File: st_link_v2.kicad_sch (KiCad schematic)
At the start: 17 parts, among them SW401 STLINK_RST, U401 STM32F103CBTx, Y401 8MHz (7pF)

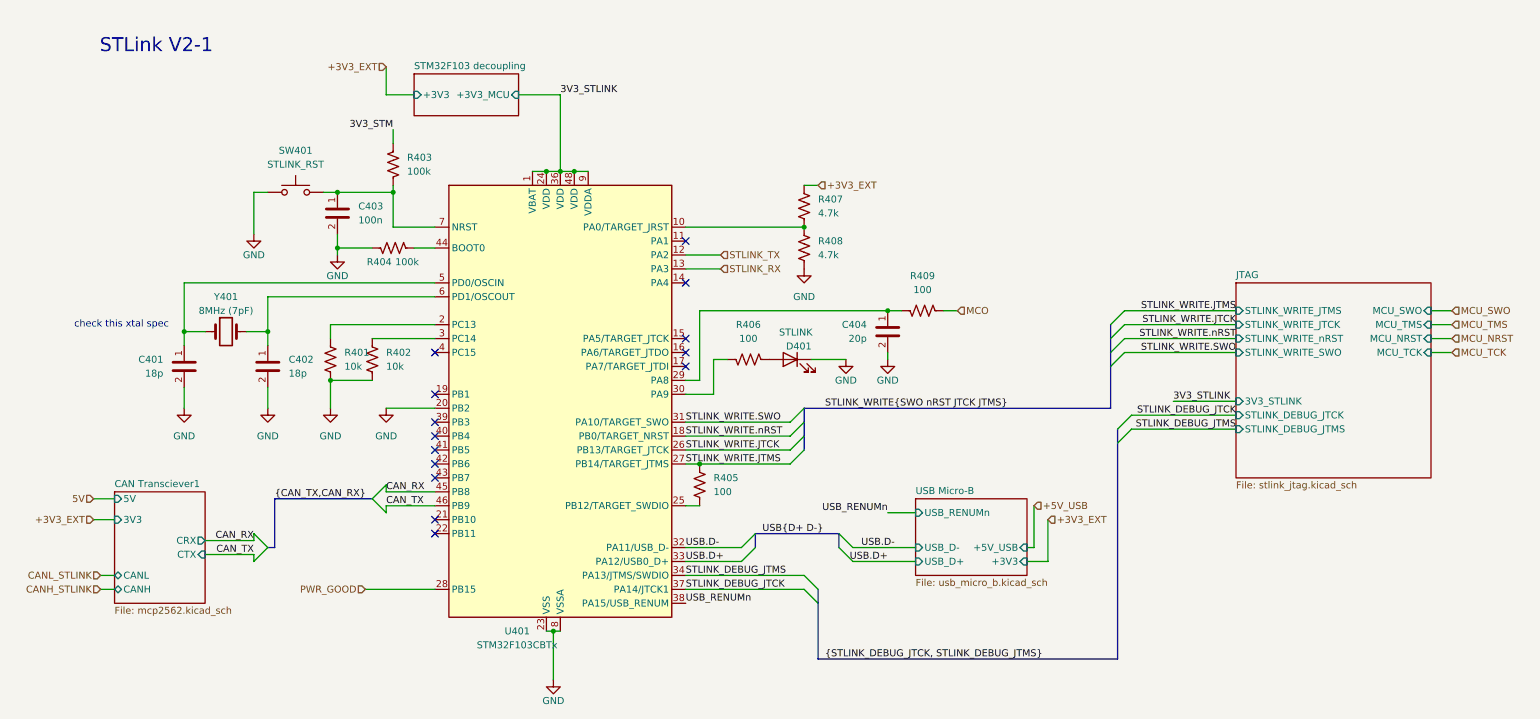
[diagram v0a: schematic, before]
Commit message: jk im stupid forgot to route the flash
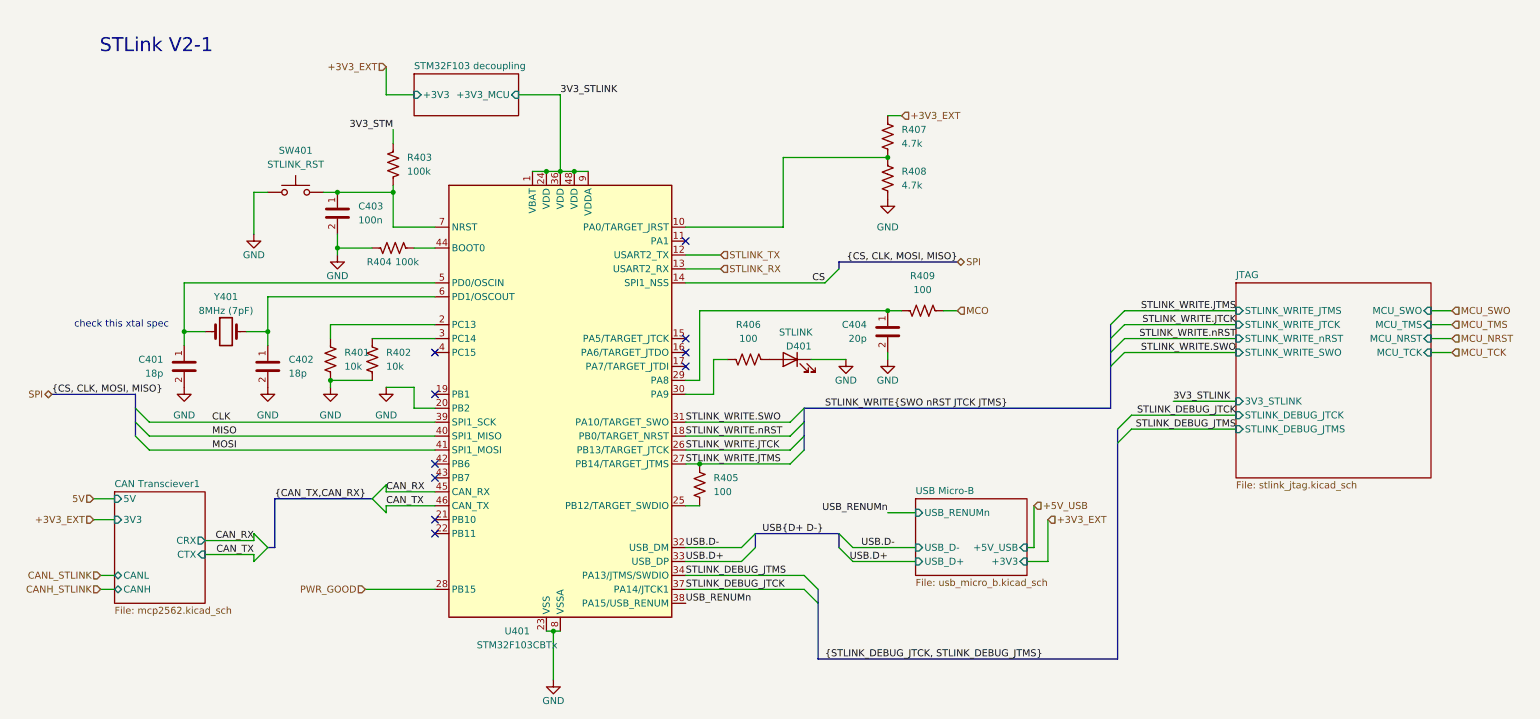
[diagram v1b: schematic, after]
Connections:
- net CS: now reaches U401.14 (PA4)
- net CLK: now reaches U401.39 (PB3)
- net MISO: now reaches U401.40 (PB4)
- net MOSI: now reaches U401.41 (PB5)
- no-connect marks 14 -> 10
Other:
- moved on the sheet: R407, R408

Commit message: fixed like a bunch of things, power and new xcvr and lights and other goodies, also started layout
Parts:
- removed Y401: 8MHz (7pF), Crystal:Crystal_HC49-4H_Vertical, symbol Device:Crystal
- added Y401: 8MHz 5pF, Crystal:Crystal_SMD_5032-2Pin_5.0x3.2mm_HandSoldering, symbol bfr_utilities:407F39E008M0000
- SW401: footprint (none) -> Button_Switch_SMD:SW_Push_1P1T-SH_NO_CK_KMR2xxG
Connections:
- net at C402.1, U401.6 (PD1/OSCOUT): now also Y401.2
- net at C401.1, U401.5 (PD0/OSCIN): now also Y401.1
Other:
- sheet CAN Transciever1 ports: added none; removed 5V
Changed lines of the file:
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@@
 	(wire
 		(pts
-			(xy 26.67 109.22) (xy 30.48 109.22)
-		)
-		(stroke
-			(width 0)
-			(type default)
-		)
-	)
-	(wire
-		(pts
 			(xy 152.4 46.99) (xy 171.45 46.99)
 		)
@@
 		)
 	)
-	(hierarchical_label "5V"
-		(shape input)
-		(at 26.67 109.22 180)
-		(effects
-			(font
-				(size 1.27 1.27)
-			)
-			(justify right)
-		)
-	)
 	(hierarchical_label "+3V3_EXT"
 		(shape input)
@@
 		(on_board yes)
 		(dnp no)
-		(property "Reference" "#PWR0409"
+		(property "Reference" "#PWR0408"
 			(at 163.83 90.17 0)
 			(effects
@@
 			(project "DU UC V1 - Minnow"
 				(path "/0aeff2df-21bc-4c76-95d6-83ff8577a8db/39f2e686-5d02-49cd-becc-d2ee5e3525ad"
-					(reference "#PWR0409")
+					(reference "#PWR0408")
 					(unit 1)
 				)
@@
 		(dnp no)
 		(fields_autoplaced yes)
-		(property "Reference" "#PWR0408"
+		(property "Reference" "#PWR0409"
 			(at 171.45 60.96 0)
 			(effects
@@
 			(project "DU UC V1 - Minnow"
 				(path "/0aeff2df-21bc-4c76-95d6-83ff8577a8db/39f2e686-5d02-49cd-becc-d2ee5e3525ad"
-					(reference "#PWR0408")
+					(reference "#PWR0409")
 					(unit 1)
 				)
@@
 			)
 		)
-		(property "Footprint" ""
+		(property "Footprint" "Button_Switch_SMD:SW_Push_1P1T-SH_NO_CK_KMR2xxG"
 			(at 63.5 48.26 0)
 			(effects
@@
 	)
 	(symbol
-		(lib_id "Device:Crystal")
-		(at 50.8 78.74 0)
-		(unit 1)
-		(exclude_from_sim no)
-		(in_bom yes)
-		(on_board yes)
-		(dnp no)
-		(property "Reference" "Y401"
-			(at 50.8 72.39 0)
-			(effects
-				(font
-					(size 1.27 1.27)
-				)
-			)
-		)
-		(property "Value" "8MHz (7pF)"
-			(at 50.8 74.93 0)
-			(effects
-				(font
-					(size 1.27 1.27)
-				)
-			)
-		)
-		(property "Footprint" "Crystal:Crystal_HC49-4H_Vertical"
-			(at 50.8 78.74 0)
-			(effects
-				(font
-					(size 1.27 1.27)
-				)
-				(hide yes)
-			)
-		)
-		(property "Datasheet" "https://www.mouser.com/datasheet/2/3/ABL2-1670425.pdf"
-			(at 50.8 78.74 0)
-			(effects
-				(font
-					(size 1.27 1.27)
-				)
-				(hide yes)
-			)
-		)
-		(property "Description" "Two pin crystal"
-			(at 50.8 78.74 0)
-			(effects
-				(font
-					(size 1.27 1.27)
-				)
-				(hide yes)
-			)
-		)
-		(property "Digikey P/N" "3155-8M20P2/49US-ND "
-			(at 50.8 78.74 0)
-			(effects
-				(font
-					(size 1.27 1.27)
-				)
-				(hide yes)
-			)
-		)
-		(property "Manufacturer P/N" "ABL2-8.000MHZ-D3W-I-T "
-			(at 50.8 78.74 0)
-			(effects
-				(font
-					(size 1.27 1.27)
-				)
-				(hide yes)
-			)
-		)
-		(property "Field7" ""
-			(at 50.8 78.74 0)
-			(effects
-				(font
-					(size 1.27 1.27)
-				)
-				(hide yes)
-			)
-		)
-		(property "JLCPCB Basic Part" "No"
-			(at 50.8 78.74 0)
-			(effects
-				(font
-					(size 1.27 1.27)
-				)
-				(hide yes)
-			)
-		)
-		(property "Mouser P/N" "815-ABL28MHZD3WIT"
-			(at 50.8 78.74 0)
-			(effects
-				(font
-					(size 1.27 1.27)
-				)
-				(hide yes)
-			)
-		)
-		(property "Order From" "Mouser"
-			(at 50.8 78.74 0)
-			(effects
-				(font
-					(size 1.27 1.27)
-				)
-				(hide yes)
-			)
-		)
-		(pin "1"
-		)
-		(pin "2"
-		)
-		(instances
-			(project "DU UC V1 - Minnow"
-				(path "/0aeff2df-21bc-4c76-95d6-83ff8577a8db/39f2e686-5d02-49cd-becc-d2ee5e3525ad"
-					(reference "Y401")
-					(unit 1)
-				)
-			)
-			(project "STM32F446 breakout V1 - Garibaldi"
-				(path "/6c37e641-6488-4ca1-9b36-326ba4e05a40/e3e74f47-7470-4558-b6f7-5225f0dc3823"
-					(reference "Y3")
-					(unit 1)
-				)
-			)
-		)
-	)
-	(symbol
 		(lib_id "bfr_resistors:RMCF0402FT100R")
 		(at 177.8 74.93 0)
@@
 	)
 	(symbol
+		(lib_id "bfr_utilities:407F39E008M0000")
+		(at 50.8 78.74 0)
+		(unit 1)
+		(exclude_from_sim no)
+		(in_bom yes)
+		(on_board yes)
+		(dnp no)
+		(fields_autoplaced yes)
+		(property "Reference" "Y401"
+			(at 50.8 71.12 0)
+			(effects
+				(font
+					(size 1.27 1.27)
+				)
+			)
+		)
+		(property "Value" "8MHz 5pF"
+			(at 50.8 73.66 0)
+			(effects
+				(font
+					(size 1.27 1.27)
+				)
+			)
+		)
+		(property "Footprint" "Crystal:Crystal_SMD_5032-2Pin_5.0x3.2mm_HandSoldering"
+			(at 50.8 78.74 0)
+			(effects
+				(font
+					(size 1.27 1.27)
+				)
+				(hide yes)
+			)
+		)
+		(property "Datasheet" "https://jlcpcb.com/api/file/downloadByFileSystemAccessId/8579709271493435392"
+			(at 50.8 78.74 0)
+			(effects
+				(font
+					(size 1.27 1.27)
+				)
+				(hide yes)
+			)
+		)
+		(property "Description" "SMD-2 Crystal, 8MHz, 5pF C_0, 20pF C_L, 80R ESR, 20ppm"
+			(at 50.8 78.74 0)
+			(effects
+				(font
+					(size 1.27 1.27)
+				)
+				(hide yes)
+			)
+		)
+		(property "Digikey P/N" "4309-XC53G2-8.000-F20LJDTKCS-ND"
+			(at 50.8 78.74 0)
+			(effects
+				(font
+					(size 1.27 1.27)
+				)
+				(hide yes)
+			)
+		)
+		(property "Manufacturer P/N" "AS-16.000-18-SMD-TR"
+			(at 50.8 78.74 0)
+			(effects
+				(font
+					(size 1.27 1.27)
+				)
+				(hide yes)
+			)
+		)
+		(property "Mouser P/N" ""
+			(at 50.8 78.74 0)
+			(effects
+				(font
+					(size 1.27 1.27)
+				)
+				(hide yes)
+			)
+		)
+		(property "Manufacturer" "Raltron Electronics"
+			(at 50.8 78.74 0)
+			(effects
+				(font
+					(size 1.27 1.27)
+				)
+				(hide yes)
+			)
+		)
+		(property "LCSC P/N" "C115962"
+			(at 50.8 78.74 0)
+			(effects
+				(font
+					(size 1.27 1.27)
+				)
+				(hide yes)
+			)
+		)
+		(property "JLC Basic?" "Yes"
+			(at 50.8 78.74 0)
+			(effects
+				(font
+					(size 1.27 1.27)
+				)
+				(hide yes)
+			)
+		)
+		(property "Order From" "JLC"
+			(at 50.8 78.74 0)
+			(effects
+				(font
+					(size 1.27 1.27)
+				)
+				(hide yes)
+			)
+		)
+		(property "JLC Basic Part" "No"
+			(at 50.8 78.74 0)
+			(effects
+				(font
+					(size 1.27 1.27)
+				)
+				(hide yes)
+			)
+		)
+		(property "Created By" "Manual Entry"
+			(at 50.8 78.74 0)
+			(effects
+				(font
+					(size 1.27 1.27)
+				)
+				(hide yes)
+			)
+		)
+		(pin "1"
+		)
+		(pin "2"
+		)
+		(instances
+			(project ""
+				(path "/0aeff2df-21bc-4c76-95d6-83ff8577a8db/39f2e686-5d02-49cd-becc-d2ee5e3525ad"
+					(reference "Y401")
+					(unit 1)
+				)
+			)
+		)
+	)
+	(symbol
 		(lib_id "bfr_capacitors:CL05B104KB54PNC")
 		(at 71.12 57.15 0)
@@
 			(effects
 				(font
-					(size 1.27 1.27)
-				)
-				(justify left)
-			)
-		)
-		(pin "5V" input
-			(at 30.48 109.22 180)
-			(effects
-				(font

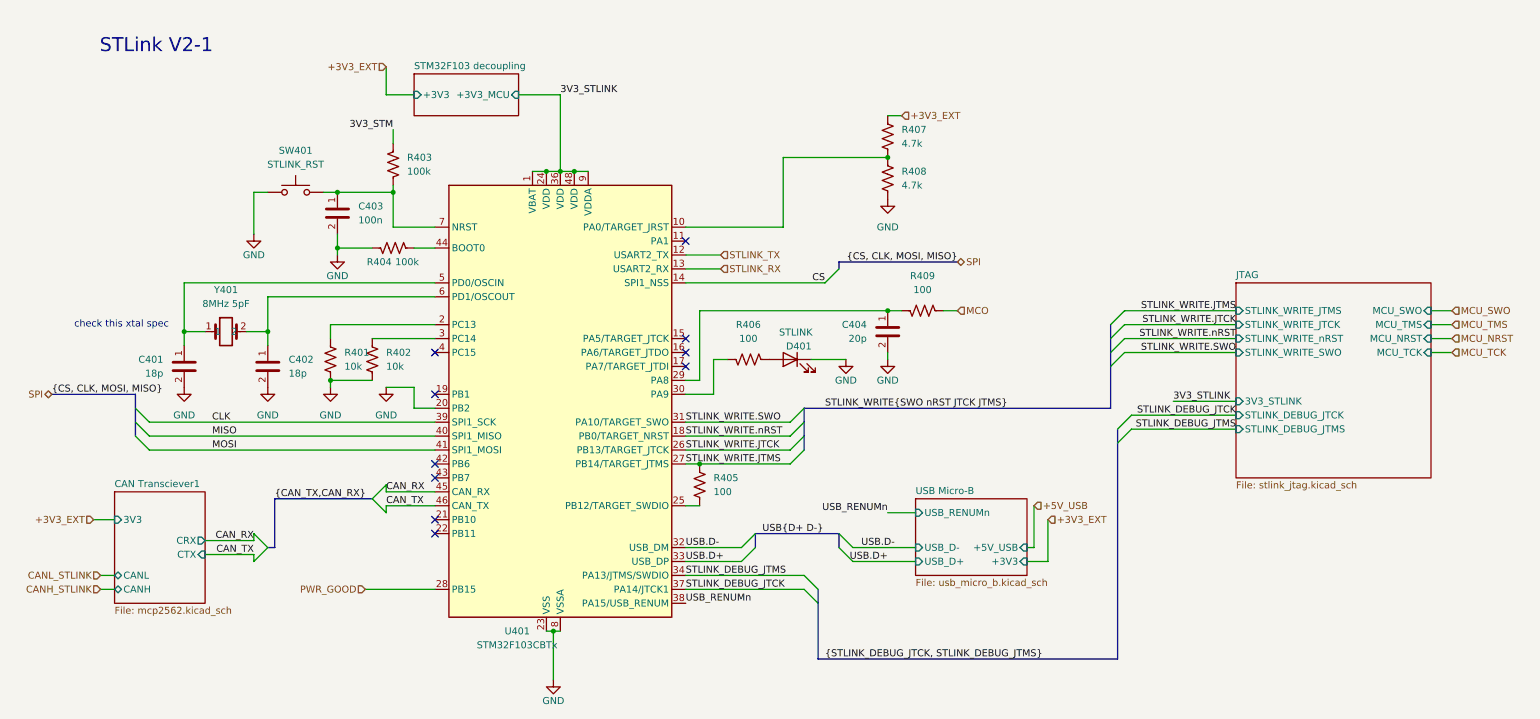
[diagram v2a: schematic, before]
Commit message: laid out most of power, main xcvr, prob some other stuff
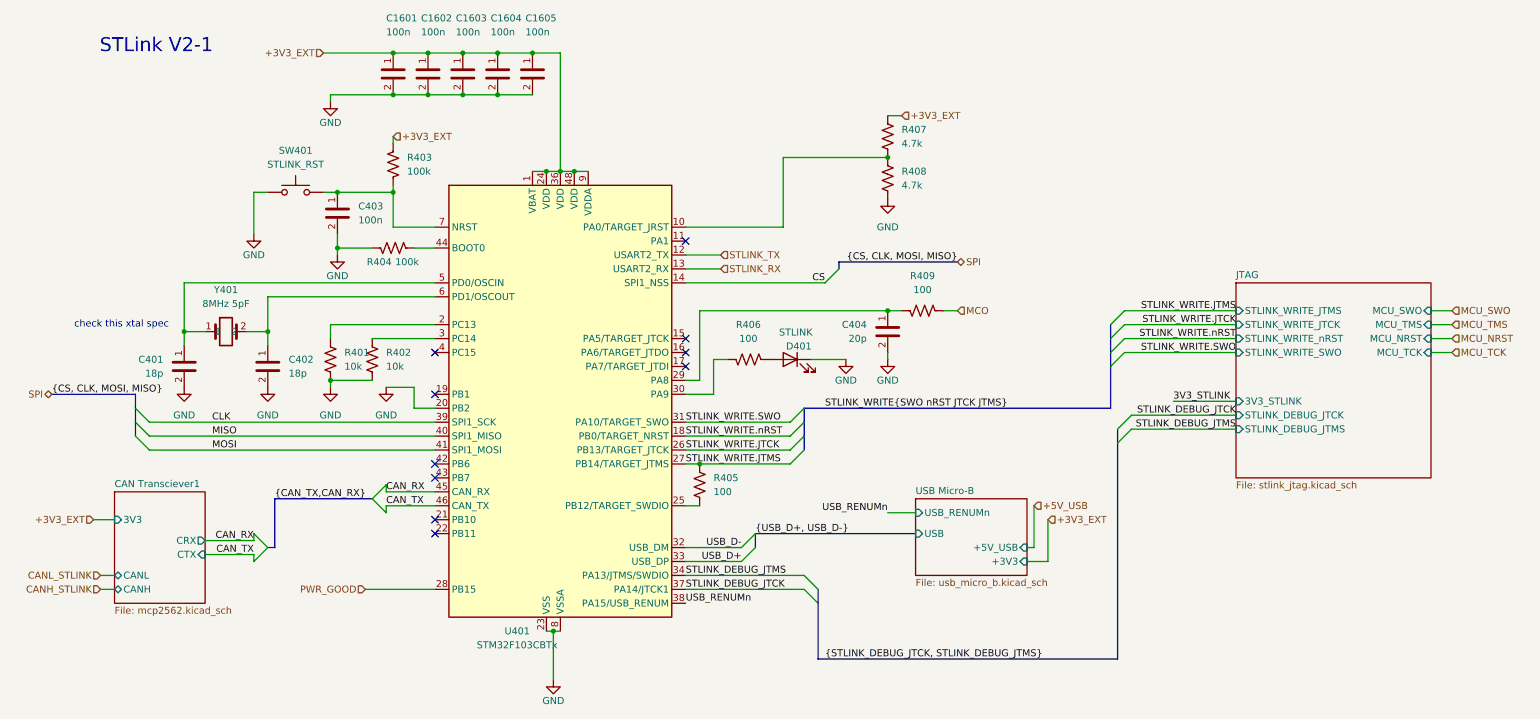
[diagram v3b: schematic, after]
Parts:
- added C1601, C1602, C1603, C1604, C1605: 100n, Capacitor_SMD:C_0402_1005Metric_Pad0.74x0.62mm_HandSolder, symbol bfr_capacitors:CL05B104KB54PNC
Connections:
- net 3V3_STM is gone; now on net +3V3_EXT: R403.2
- net +3V3_EXT: now also U401.1 (VBAT), U401.24 (VDD), U401.36 (VDD), U401.48 (VDD), U401.9 (VDDA), C1601.1, C1602.1, C1603.1, C1604.1, C1605.1
- net 3V3_STLINK: no longer U401.1 (VBAT), U401.24 (VDD), U401.36 (VDD), U401.48 (VDD), U401.9 (VDDA)
- net GND: now also C1601.2, C1602.2, C1603.2, C1604.2, C1605.2
- net USB.D+ renamed USB_D+
- net USB.D- renamed USB_D-
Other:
- removed sheet STM32F103 decoupling
- sheet USB Micro-B ports: added USB; removed USB_D+, USB_D-

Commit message: i fucken rerouted everything and redid the pinout like 3x, half routed GPIOs
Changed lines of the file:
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@@
 		)
 	)
-	(hierarchical_label "CANH_STLINK"
+	(hierarchical_label "STLINK_CAN+"
 		(shape input)
 		(at 27.94 125.73 180)
@@
 		)
 	)
-	(hierarchical_label "CANL_STLINK"
+	(hierarchical_label "STLINK_CAN-"
 		(shape input)
 		(at 27.94 123.19 180)

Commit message: fucking shit bro i like expanded the board by 1mm and it still has no room fuck this bitchass crystal
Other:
- sheet JTAG ports: added +5V; removed none
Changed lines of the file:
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@@
 	(wire
 		(pts
-			(xy 274.32 82.55) (xy 270.51 82.55)
+			(xy 274.32 96.52) (xy 270.51 96.52)
 		)
 		(stroke
@@
 	(wire
 		(pts
-			(xy 274.32 74.93) (xy 270.51 74.93)
+			(xy 274.32 88.9) (xy 270.51 88.9)
 		)
 		(stroke
@@
 	(wire
 		(pts
-			(xy 274.32 77.47) (xy 270.51 77.47)
+			(xy 274.32 91.44) (xy 270.51 91.44)
 		)
 		(stroke
@@
 	(wire
 		(pts
+			(xy 273.05 77.47) (xy 270.51 77.47)
+		)
+		(stroke
+			(width 0)
+			(type default)
+		)
+	)
+	(wire
+		(pts
 			(xy 81.28 53.34) (xy 81.28 59.69)
 		)
@@
 	(wire
 		(pts
-			(xy 274.32 80.01) (xy 270.51 80.01)
+			(xy 274.32 93.98) (xy 270.51 93.98)
 		)
 		(stroke
@@
 	(hierarchical_label "MCU_SWO"
 		(shape input)
-		(at 274.32 74.93 0)
+		(at 274.32 88.9 0)
 		(effects
 			(font
@@
 	(hierarchical_label "MCU_TCK"
 		(shape input)
-		(at 274.32 82.55 0)
+		(at 274.32 96.52 0)
 		(effects
 			(font
@@
 	(hierarchical_label "MCU_TMS"
 		(shape input)
-		(at 274.32 77.47 0)
+		(at 274.32 91.44 0)
 		(effects
 			(font
@@
 		)
 	)
+	(hierarchical_label "+5V_USB"
+		(shape input)
+		(at 273.05 77.47 0)
+		(effects
+			(font
+				(size 1.27 1.27)
+			)
+			(justify left)
+		)
+	)
 	(hierarchical_label "+3V3_EXT"
 		(shape input)
@@
 	(hierarchical_label "MCU_NRST"
 		(shape input)
-		(at 274.32 80.01 0)
+		(at 274.32 93.98 0)
 		(effects
 			(font
@@
 		)
 		(pin "MCU_SWO" input
-			(at 270.51 74.93 0)
+			(at 270.51 88.9 0)
 			(effects
 				(font
@@
 		)
 		(pin "MCU_TMS" input
-			(at 270.51 77.47 0)
+			(at 270.51 91.44 0)
 			(effects
 				(font
@@
 		)
 		(pin "MCU_NRST" input
-			(at 270.51 80.01 0)
+			(at 270.51 93.98 0)
 			(effects
 				(font
@@
 		)
 		(pin "MCU_TCK" input
-			(at 270.51 82.55 0)
+			(at 270.51 96.52 0)
 			(effects
 				(font
@@
 			)
 		)
+		(pin "+5V" input
+			(at 270.51 77.47 0)
+			(effects
+				(font
+					(size 1.27 1.27)
+				)
+				(justify right)
+			)
+		)
